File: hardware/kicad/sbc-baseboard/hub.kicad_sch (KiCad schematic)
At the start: 84 parts, among them J1 USB-C upstream, J4 USB-A PORT1, J5 USB-A PORT3, U401 USBLC6-2SC6, U402 USB2517, U403 TPS2553DBV, U404 TPS2553DBV, U405 TPS2553DBV, U406 TPS2553DBV, U407 TPS2553DBV, U408 USBLC6-2SC6, U409 USBLC6-2SC6, U410 USBLC6-2SC6, U411 USBLC6-2SC6, Y401 24MHz

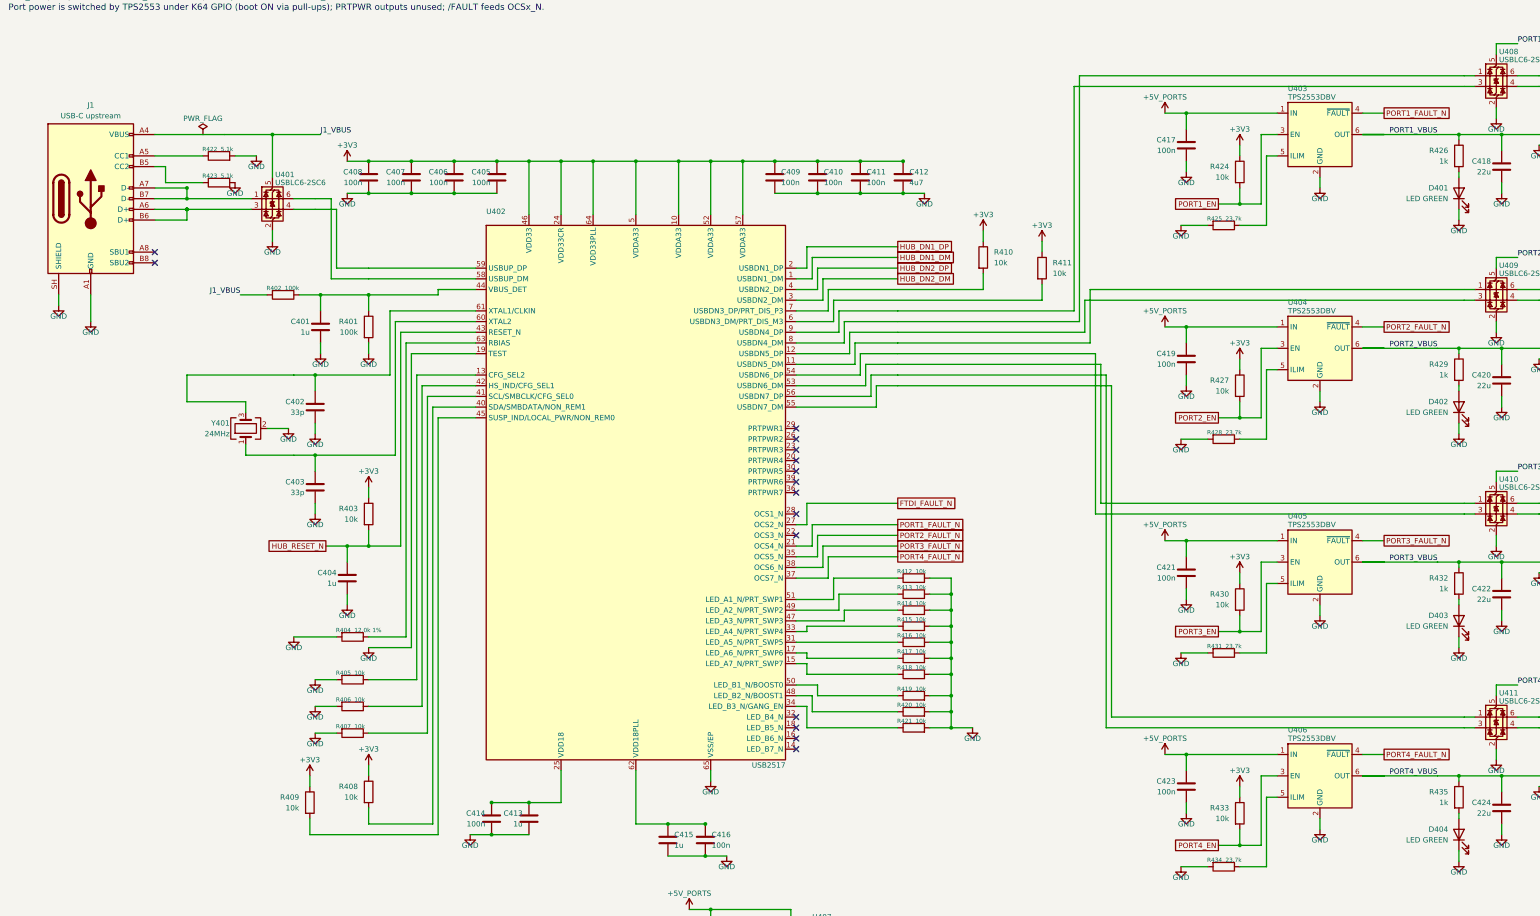
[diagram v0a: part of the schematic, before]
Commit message: Clock sources flow downward; USB pairs ordered as on the ESD array
Every crystal is now drawn by one helper: the two XTAL lanes run out past
the side's route channels to two columns 7.62 mm apart, drop at right
angles through the crystal lying across them, on into one load capacitor
each and a shared GND rail with one GND symbol, which also takes the
crystal's ground pins. The capacitors no longer hang off the lanes beside
the hub with the crystal somewhere else; nothing crosses.

Library v0.2.2: USB pairs are listed D- above D+, the order of the lines
through a USBLC6 array, so J3/U202 now sit on the K64's USB rows with
straight wires and the hub's upstream routes no longer cross; the hub's XTAL
pins move to the bottom of its left column so the clock cluster hangs under
everything else there, with clear rows around VBUS_DET.

All sheets: ERC 0, contacts 0, merges 0, layout 0; connectivity unchanged.

Co-Authored-By: Claude Fable 5.1 <noreply@anthropic.com>
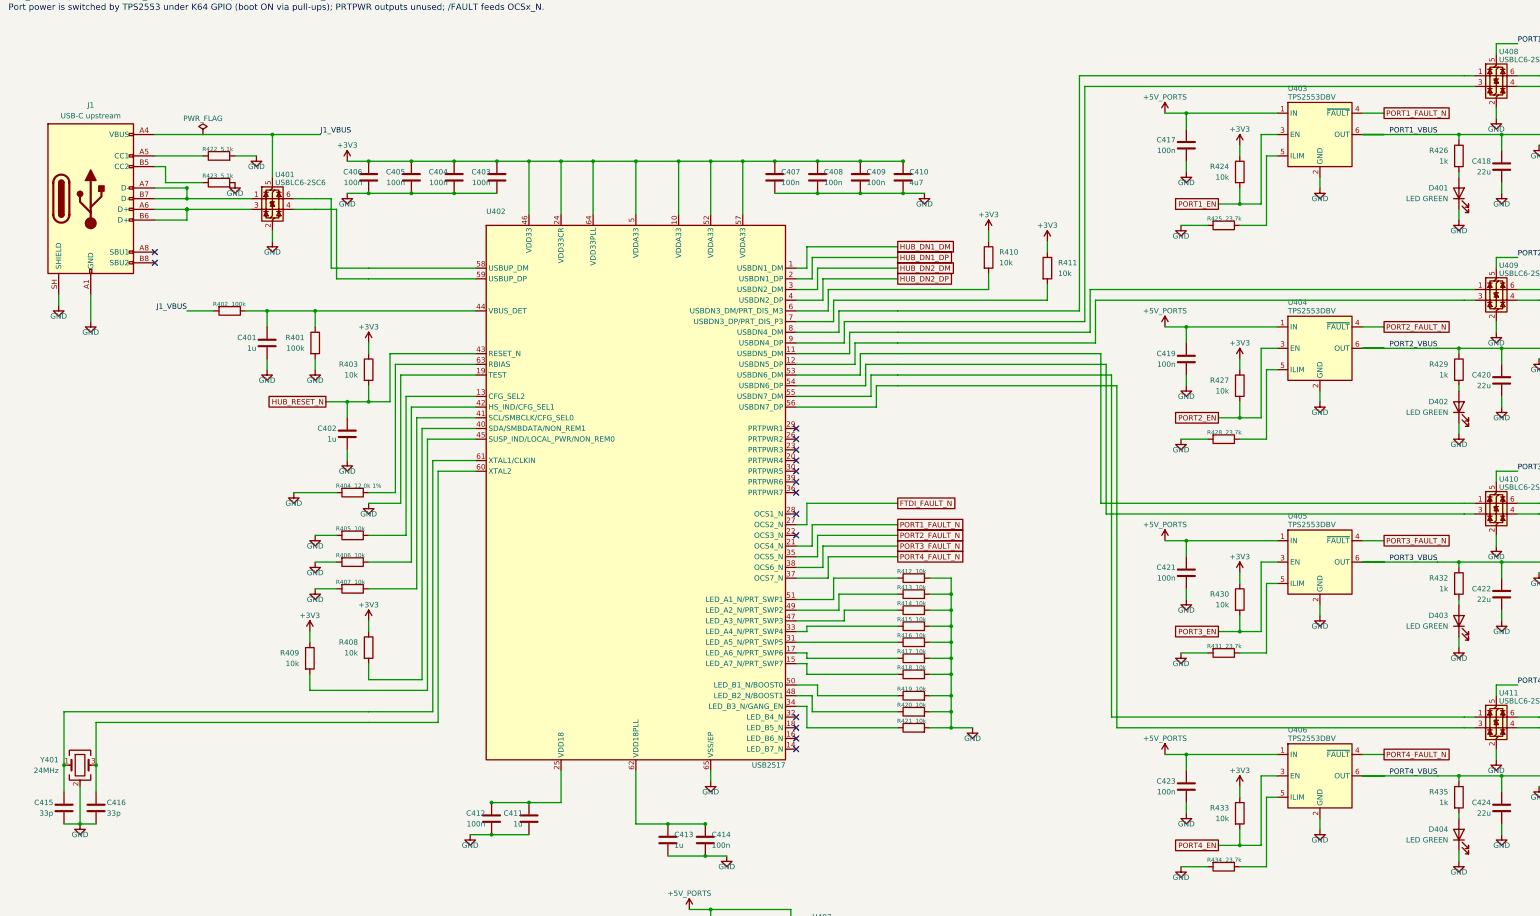
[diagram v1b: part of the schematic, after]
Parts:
- C402: value 33p -> 1u
- C403: value 33p -> 100n
- C404: value 1u -> 100n
- C410: value 100n -> 4u7; footprint Capacitor_SMD:C_0603_1608Metric -> Capacitor_SMD:C_0805_2012Metric
- C411: value 100n -> 1u
- C412: value 4u7 -> 100n; footprint Capacitor_SMD:C_0805_2012Metric -> Capacitor_SMD:C_0603_1608Metric
- C415: value 1u -> 33p
- C416: value 100n -> 33p
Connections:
- net +3V3: now also C403.1, C404.1; no longer C411.1, C412.1
- net HUB_RESET_N: now also C402.1; no longer C404.1
- net at U402.6 (USBDN3_DM/PRT_DIS_M3): now also R410.2; no longer R411.2
- net at C413.1, C414.1: now also U402.62 (VDD18PLL); no longer U402.25 (VDD18)
- net at U402.7 (USBDN3_DP/PRT_DIS_P3): now also R411.2; no longer R410.2
- new net: C415.1, U402.61 (XTAL1/CLKIN), Y401.1
- new net: C416.1, U402.60 (XTAL2), Y401.3
- new net: C411.1, C412.1, U402.25 (VDD18)

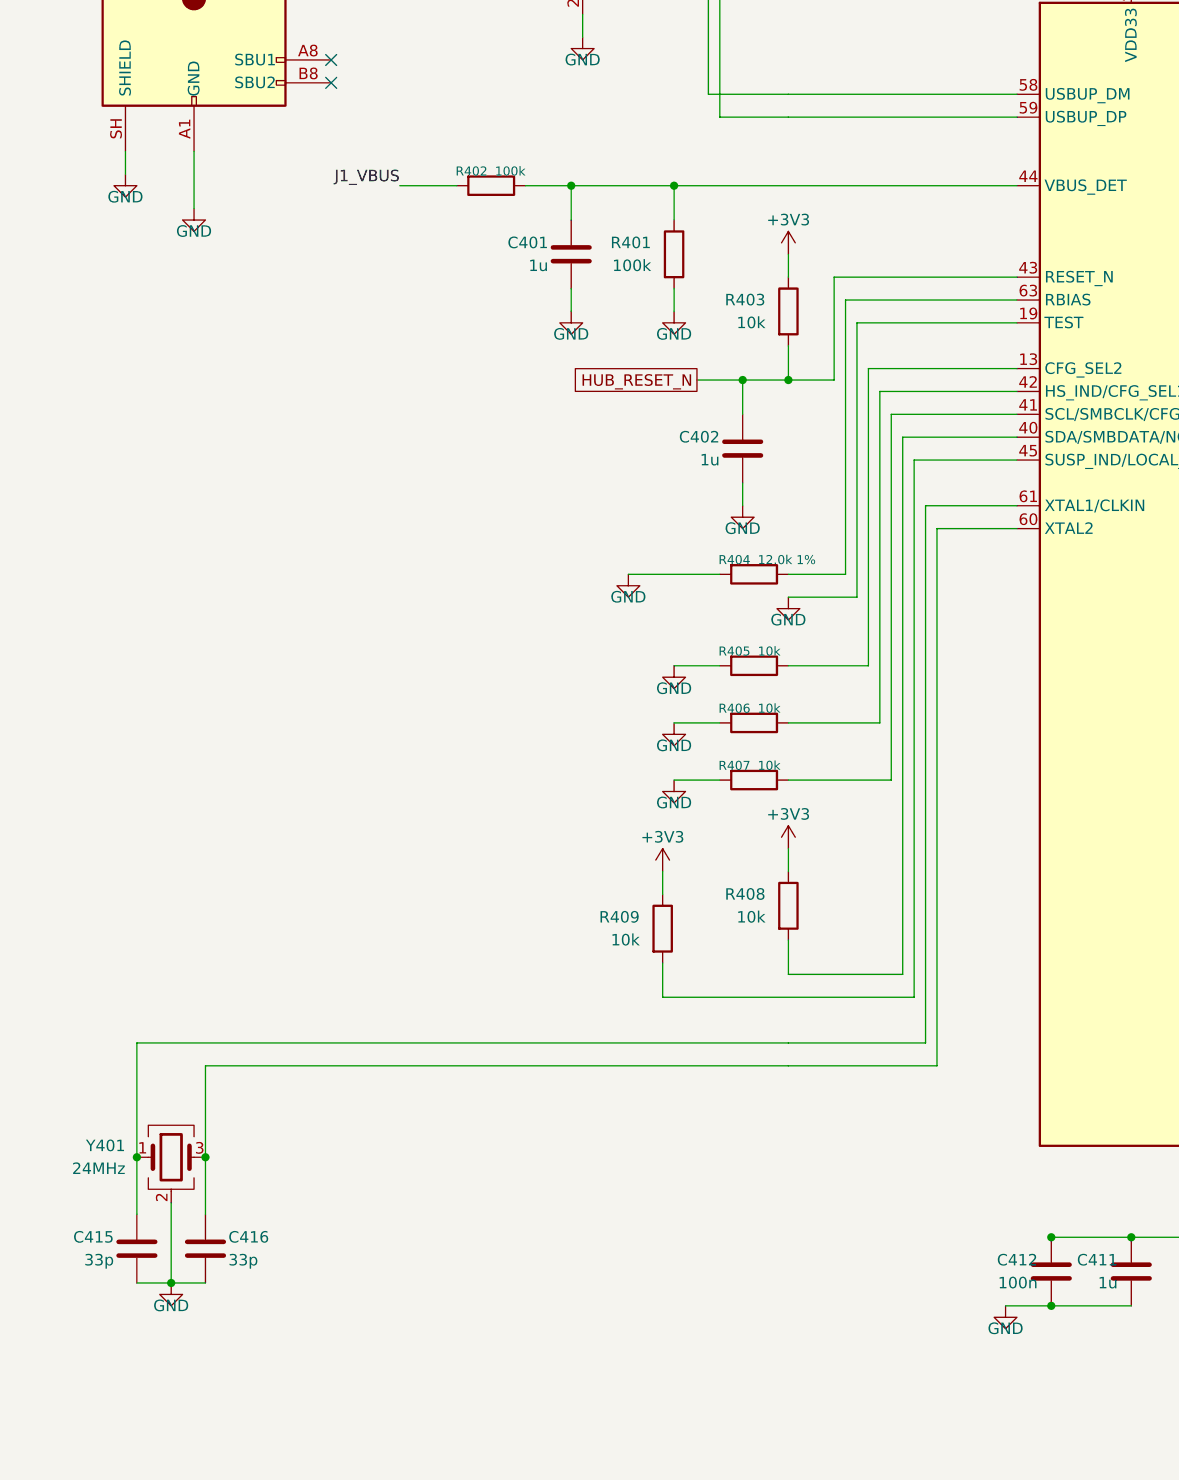
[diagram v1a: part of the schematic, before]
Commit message: Reset circuits flow downward: pull-up, capacitor and button in one cluster
A Reset attachment in the fan engine draws the network at the lane end, top to
bottom: rail symbol, pull-up, the node row where the lane arrives, the capacitor
straight below in the same column, one GND under it; a push button hangs from
the lane one column nearer the hub and shares the GND rail. It declares its
reaches, so the spread and slide passes keep the neighbouring rows clear. Used
for the K64 (RESET), the USB2517 and the K20 (DAP RESET); the K20's SWD header
takes the K20_RESET_N label instead of a fourth wire into the node. Netlist
membership unchanged (356 nets); ERC, geometry, connectivity and layout gates
all at zero.

Co-Authored-By: Claude Fable 5.1 <noreply@anthropic.com>
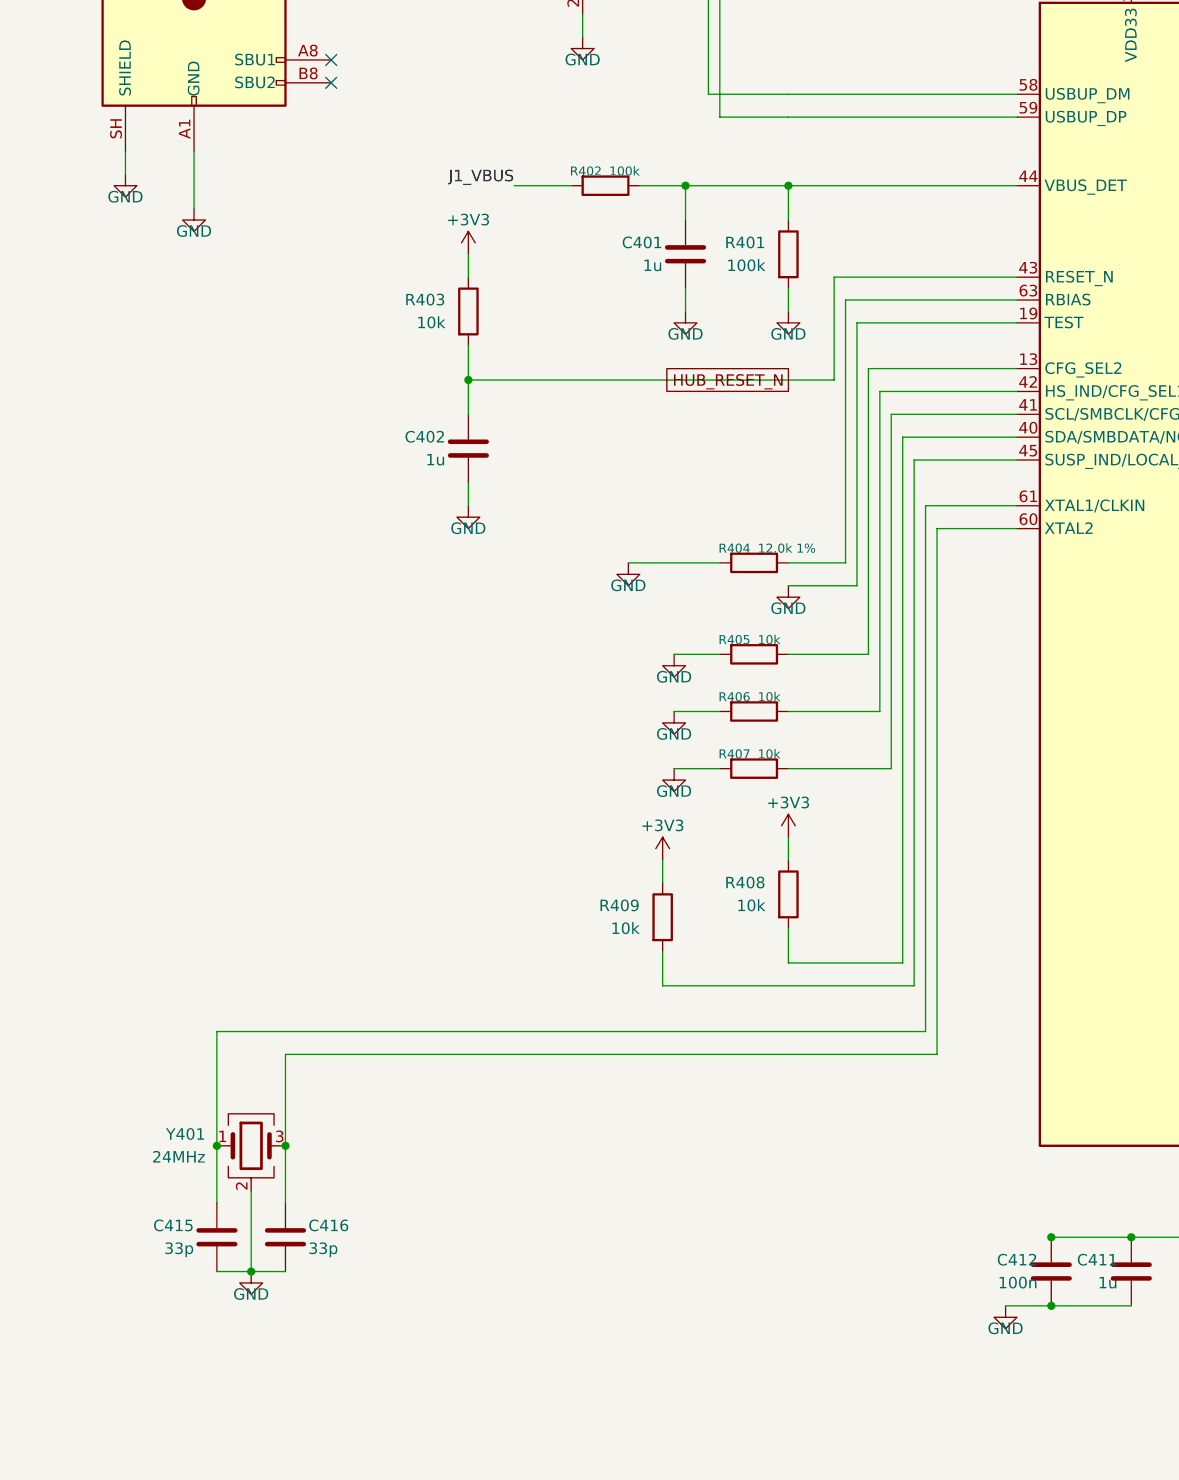
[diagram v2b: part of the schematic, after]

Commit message: Derived UUIDs and pinned export dates: builds are reproducible
Every UUID is a UUID5 in a namespace made from the project name, keyed by what
the element is (symbol: reference and unit; pin: its symbol; wire: sheet and
ends; label: sheet, net and position; sheet: file name; identical keys get a
counter in draw order). The ERC report header and the PDF creation date are
pinned to the title-block date. Two builds of one design now give byte-identical
files; no duplicate UUIDs across 4477. The BOM export is back in the build.

Also: one Value for both units of each stacked USB-A connector. KiCad treated
the differing unit values as an annotation error on every netlist export and
listed them as 'USB-A PORT1,USB-A PORT2' in the BOM; the ports are identified by
J4A/J4B and J5A/J5B and the sheet note. Netlist membership unchanged.

Co-Authored-By: Claude Fable 5.1 <noreply@anthropic.com>
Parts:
- J4: value USB-A PORT1 -> USB-A x2
- J4: value USB-A PORT2 -> USB-A x2
- J5: value USB-A PORT3 -> USB-A x2
- J5: value USB-A PORT4 -> USB-A x2
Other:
- note added: "Port map: 1 = DAPLink, 2 = FT231X, 3 = disabled (DN3 pulled up), 4..7 = USB-A PORT1..PORT4 (J4A/J4B = PORT1/PORT2 on hub ports 4,5; J5A/J5B = PORT3/PORT4 on ports 6,7)."
- note removed: "Port map: 1 = DAPLink, 2 = FT231X, 3 = disabled (DN3 pulled up), 4..7 = USB-A PORT1..PORT4 (J4: ports 4,5; J5: ports 6,7)."

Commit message: USB 2.0 differential pairs named for the router; USB net class; ports aligned
Every USB 2.0 data net is now <base>_P / <base>_N, the suffixes KiCad's PCB
editor pairs up: J1_D, J3_D, PORT1_D..PORT4_D on the receptacle side of each
ESD array; HUB_UP and HUB_DN1..HUB_DN7 at the hub; K64_USB and FTDI_USB at the
chips. All 15 pairs are complete with D+ on _P. The project file gains a USB
net class assigned by pattern (differential geometry to be set from the
stackup). The labels sit at wire ends with their text along the pair's own
wire; routes now run their last leg into a side pin as one wire so a label at
the pin end owns the stretch (Conn join=False keeps a shared stub where two
routes meet at one pin). The USB-A receptacles and their switches move down
1.27 mm so the pairs run straight from the ESD arrays, and the port ESD arrays
move left to make room for the labels. Netlist membership unchanged (356
nets); ERC, geometry, connectivity, layout and reproducibility gates all
clean.

Co-Authored-By: Claude Fable 5.1 <noreply@anthropic.com>
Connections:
- net HUB_DN7_N: now reaches U402.55 (USBDN7_DM), U411.1 (I/O1)
- net HUB_DN7_P: now reaches U402.56 (USBDN7_DP), U411.3 (I/O2)
- net PORT4_D_P: now reaches J5.7 (D+), U411.4 (I/O2)
- net PORT4_D_N: now reaches J5.6 (D-), U411.6 (I/O1)
- net PORT1_D_N: now reaches J4.2 (D-), U408.6 (I/O1)
- net PORT1_D_P: now reaches J4.3 (D+), U408.4 (I/O2)
- net PORT3_D_N: now reaches J5.2 (D-), U410.6 (I/O1)
- net PORT3_D_P: now reaches J5.3 (D+), U410.4 (I/O2)
- net HUB_DN5_N: now reaches U402.11 (USBDN5_DM), U409.1 (I/O1)
- net HUB_DN5_P: now reaches U402.12 (USBDN5_DP), U409.3 (I/O2)
- net HUB_DN6_N: now reaches U402.53 (USBDN6_DM), U410.1 (I/O1)
- net HUB_DN6_P: now reaches U402.54 (USBDN6_DP), U410.3 (I/O2)
- net HUB_UP_N: now reaches U401.6 (I/O1), U402.58 (USBUP_DM)
- net HUB_UP_P: now reaches U401.4 (I/O2), U402.59 (USBUP_DP)
- net HUB_DN4_N: now reaches U402.8 (USBDN4_DM), U408.1 (I/O1)
- net HUB_DN4_P: now reaches U402.9 (USBDN4_DP), U408.3 (I/O2)
- net PORT2_D_P: now reaches J4.7 (D+), U409.4 (I/O2)
- net PORT2_D_N: now reaches J4.6 (D-), U409.6 (I/O1)
- net J1_D_P: now reaches J1.A6 (D+), J1.B6 (D+), U401.3 (I/O2)
- net J1_D_N: now reaches J1.A7 (D-), J1.B7 (D-), U401.1 (I/O1)
- net HUB_DN1_DM renamed HUB_DN1_N
- net HUB_DN1_DP renamed HUB_DN1_P
- net HUB_DN2_DM renamed HUB_DN2_N
- net HUB_DN2_DP renamed HUB_DN2_P
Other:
- note added: "USB 2.0 pairs are named *_P / *_N (KiCad's differential-pair convention) and sit in net class USB: 90 ohm differential, routed as pairs, no stubs. Each ESD array splits its pair into a hub side (HUB_DNn) and a connector side (PORTn_D). Set the class's width and gap from the stackup before routing."
- moved on the sheet: C417, C418, C419, C420, C421, C422, C423, C424, D401, D402, D403, D404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
